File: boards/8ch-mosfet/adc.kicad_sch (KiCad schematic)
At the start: 13 parts, among them U13 MCP1502-33, U15 MCP3425A0T-ECH, U2 MCP3208

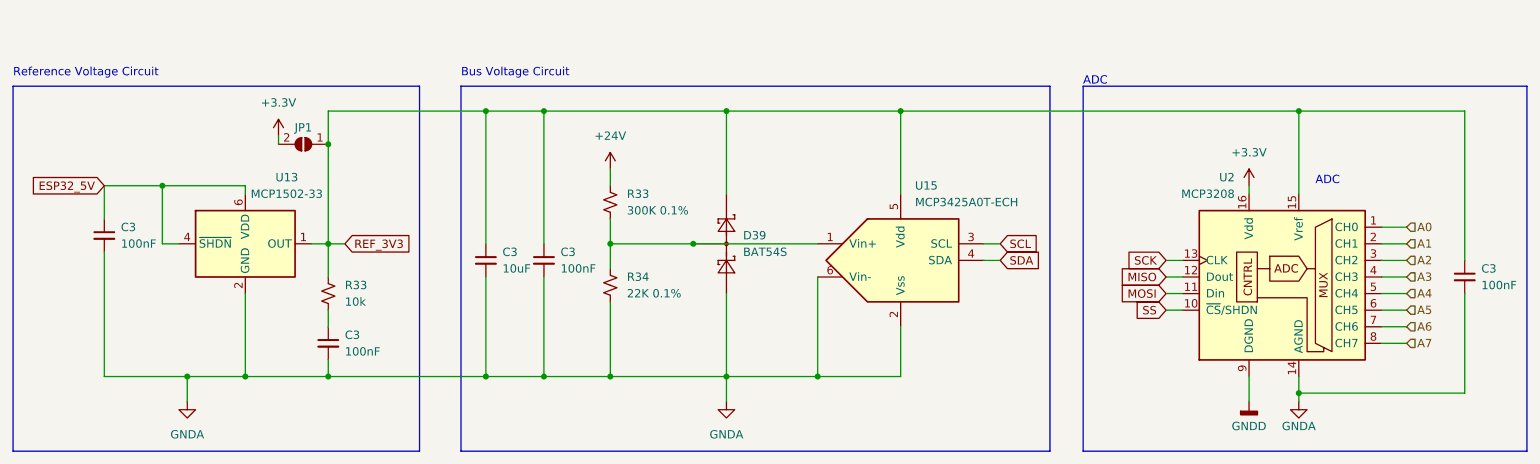
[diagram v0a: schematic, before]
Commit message: updated mosfet driver schematic with changes
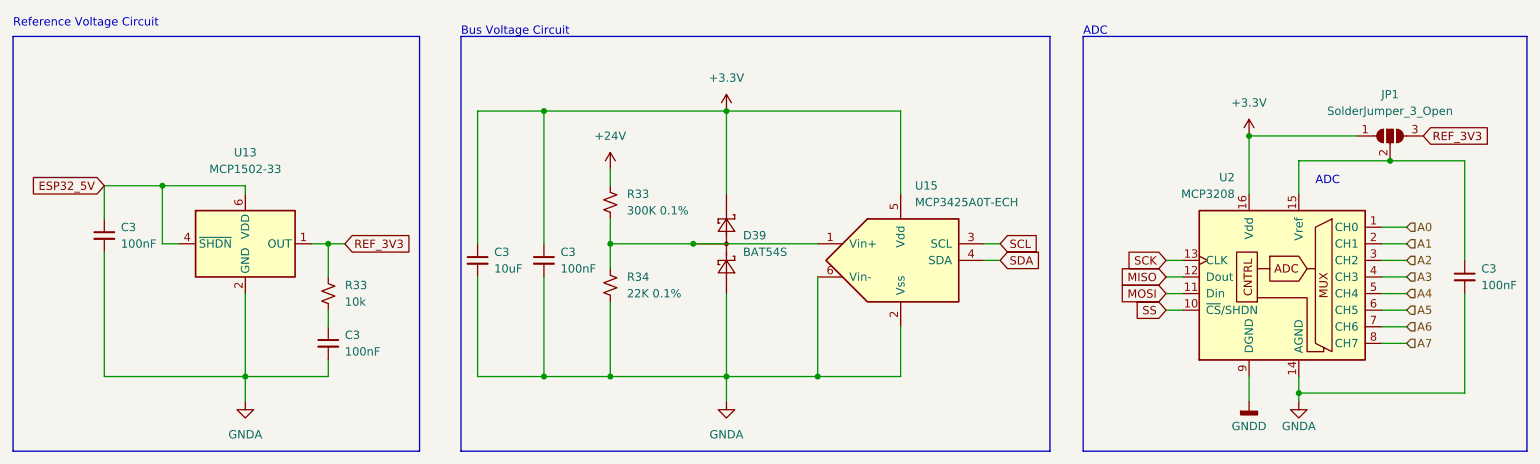
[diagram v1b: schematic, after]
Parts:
- removed JP1: SolderJumper_2_Open, Jumper:SolderJumper-2_P1.3mm_Open_RoundedPad1.0x1.5mm, symbol Jumper:SolderJumper_2_Open
- added JP1: SolderJumper_3_Open, Jumper:SolderJumper-3_P1.3mm_Open_RoundedPad1.0x1.5mm_NumberLabels, symbol Jumper:SolderJumper_3_Open
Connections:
- net +3.3V: now also C3.1, C3.1, D39.2 (K), U15.5 (Vdd), JP1.1 (A)
- net REF_3V3: now also JP1.3 (B); no longer C3.1, C3.1, C3.1, D39.2 (K), U15.5 (Vdd), U2.15 (Vref)
- new net: C3.1, JP1.2 (C), U2.15 (Vref)
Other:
- moved on the sheet: C3

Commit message: reannotated
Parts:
- renumbered D39 to D21, U13 to U18, U15 to U19
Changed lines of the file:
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@@
         )
         (path "/c83c6236-96e9-46ad-9d7a-9e2efa4a7966/b87f80e1-ecbd-4ee0-be26-4b252158928b"
-          (reference "U2") (unit 1)
+          (reference "U20") (unit 1)
         )
       )
@@
         )
         (path "/c83c6236-96e9-46ad-9d7a-9e2efa4a7966/b87f80e1-ecbd-4ee0-be26-4b252158928b"
-          (reference "#PWR07") (unit 1)
+          (reference "#PWR056") (unit 1)
         )
       )
@@
         )
         (path "/c83c6236-96e9-46ad-9d7a-9e2efa4a7966/b87f80e1-ecbd-4ee0-be26-4b252158928b"
-          (reference "#PWR03") (unit 1)
+          (reference "#PWR054") (unit 1)
         )
       )
@@
         )
         (path "/c83c6236-96e9-46ad-9d7a-9e2efa4a7966/b87f80e1-ecbd-4ee0-be26-4b252158928b"
-          (reference "#PWR070") (unit 1)
+          (reference "#PWR053") (unit 1)
         )
       )
@@
         )
         (path "/c83c6236-96e9-46ad-9d7a-9e2efa4a7966/b87f80e1-ecbd-4ee0-be26-4b252158928b"
-          (reference "R33") (unit 1)
+          (reference "R28") (unit 1)
         )
       )
@@
         )
         (path "/c83c6236-96e9-46ad-9d7a-9e2efa4a7966/b87f80e1-ecbd-4ee0-be26-4b252158928b"
-          (reference "R41") (unit 1)
+          (reference "R30") (unit 1)
         )
       )
@@
         )
         (path "/c83c6236-96e9-46ad-9d7a-9e2efa4a7966/b87f80e1-ecbd-4ee0-be26-4b252158928b"
-          (reference "#PWR058") (unit 1)
+          (reference "#PWR050") (unit 1)
         )
       )
@@
         )
         (path "/c83c6236-96e9-46ad-9d7a-9e2efa4a7966/b87f80e1-ecbd-4ee0-be26-4b252158928b"
-          (reference "C49") (unit 1)
+          (reference "C36") (unit 1)
         )
       )
@@
         )
         (path "/c83c6236-96e9-46ad-9d7a-9e2efa4a7966/b87f80e1-ecbd-4ee0-be26-4b252158928b"
-          (reference "#PWR057") (unit 1)
+          (reference "#PWR051") (unit 1)
         )
       )
@@
         )
         (path "/c83c6236-96e9-46ad-9d7a-9e2efa4a7966/b87f80e1-ecbd-4ee0-be26-4b252158928b"
-          (reference "#PWR06") (unit 1)
+          (reference "#PWR055") (unit 1)
         )
       )
@@
   (symbol (lib_id "Reference_Voltage:MCP1501-30xCH") (at 71.12 82.55 0) (unit 1)
     (in_bom yes) (on_board yes) (dnp no)
-    (property "Reference" "U13" (at 71.12 68.58 0)
+    (property "Reference" "U18" (at 71.12 68.58 0)
       (effects (font (size 1.27 1.27)))
     )
@@
       (project "8ch-mosfet"
         (path "/c83c6236-96e9-46ad-9d7a-9e2efa4a7966/b87f80e1-ecbd-4ee0-be26-4b252158928b"
-          (reference "U13") (unit 1)
+          (reference "U18") (unit 1)
         )
       )
@@
         )
         (path "/c83c6236-96e9-46ad-9d7a-9e2efa4a7966/b87f80e1-ecbd-4ee0-be26-4b252158928b"
-          (reference "C48") (unit 1)
+          (reference "C34") (unit 1)
         )
       )
@@
         )
         (path "/c83c6236-96e9-46ad-9d7a-9e2efa4a7966/b87f80e1-ecbd-4ee0-be26-4b252158928b"
-          (reference "#PWR010") (unit 1)
+          (reference "#PWR052") (unit 1)
         )
       )
@@
         )
         (path "/c83c6236-96e9-46ad-9d7a-9e2efa4a7966/b87f80e1-ecbd-4ee0-be26-4b252158928b"
-          (reference "C30") (unit 1)
+          (reference "C37") (unit 1)
         )
       )
@@
   (symbol (lib_id "Analog_ADC:MCP3425A0T-ECH") (at 171.45 85.09 0) (unit 1)
     (in_bom yes) (on_board yes) (dnp no) (fields_autoplaced)
-    (property "Reference" "U15" (at 173.6441 73.66 0)
+    (property "Reference" "U19" (at 173.6441 73.66 0)
       (effects (font (size 1.27 1.27)) (justify left))
     )
@@
       (project "8ch-mosfet"
         (path "/c83c6236-96e9-46ad-9d7a-9e2efa4a7966/b87f80e1-ecbd-4ee0-be26-4b252158928b"
-          (reference "U15") (unit 1)
+          (reference "U19") (unit 1)
         )
       )
@@
         )
         (path "/c83c6236-96e9-46ad-9d7a-9e2efa4a7966/b87f80e1-ecbd-4ee0-be26-4b252158928b"
-          (reference "C28") (unit 1)
+          (reference "C35") (unit 1)
         )
       )
@@
         )
         (path "/c83c6236-96e9-46ad-9d7a-9e2efa4a7966/b87f80e1-ecbd-4ee0-be26-4b252158928b"
-          (reference "R34") (unit 1)
+          (reference "R29") (unit 1)
         )
       )
@@
   (symbol (lib_id "Diode:BAT54S") (at 144.78 82.55 270) (mirror x) (unit 1)
     (in_bom yes) (on_board yes) (dnp no) (fields_autoplaced)
-    (property "Reference" "D39" (at 147.32 81.28 90)
+    (property "Reference" "D21" (at 147.32 81.28 90)
       (effects (font (size 1.27 1.27)) (justify left))
     )
@@
       (project "8ch-mosfet"
         (path "/c83c6236-96e9-46ad-9d7a-9e2efa4a7966/b87f80e1-ecbd-4ee0-be26-4b252158928b"
-          (reference "D39") (unit 1)
+          (reference "D21") (unit 1)
         )
       )
@@
         )
         (path "/c83c6236-96e9-46ad-9d7a-9e2efa4a7966/b87f80e1-ecbd-4ee0-be26-4b252158928b"
-          (reference "C29") (unit 1)
-        )
-      )
+          (reference "C33") (unit 1)
+        )
+      )

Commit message: 8 channel mosfet driver also ready for proto
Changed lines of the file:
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@@
   (title_block
     (title "Yarrboard 8ch Mosfet Driver")
+    (rev "C")
     (company "https://github.com/hoeken/yarrboard")
   )
@@
   )
   (junction (at 232.41 105.41) (diameter 0) (color 0 0 0 0)
+  )
+  (junction (at 232.41 69.85) (diameter 0) (color 0 0 0 0)
   )
   (junction (at 127 102.87) (diameter 0) (color 0 0 0 0)
@@
         )
       )
+    )
+  )
+  (symbol (lib_id "power:PWR_FLAG") (at 232.41 69.85 0) (unit 1)
+    (in_bom yes) (on_board yes) (dnp no)
+    (property "Reference" "#FLG04" (at 232.41 67.945 0)
+      (effects (font (size 1.27 1.27)) hide)
+    )
+    (property "Value" "PWR_FLAG" (at 232.41 71.12 0)
+      (effects (font (size 1.27 1.27)))
+    )
+    (property "Footprint" "" (at 232.41 69.85 0)
+      (effects (font (size 1.27 1.27)) hide)
+    )
+    (property "Datasheet" "~" (at 232.41 69.85 0)
+      (effects (font (size 1.27 1.27)) hide)
+    )
+    (pin "1")
+    (instances
+      (project "8ch-mosfet"
+        (path "/c83c6236-96e9-46ad-9d7a-9e2efa4a7966/e112a34f-fd2f-43cb-bf5d-a7f5e57b6bef"
+          (reference "#FLG04") (unit 1)
+        )
+        (path "/c83c6236-96e9-46ad-9d7a-9e2efa4a7966/b87f80e1-ecbd-4ee0-be26-4b252158928b"
+          (reference "#FLG010") (unit 1)
+        )
+      )

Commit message: first commit of the 'totem pole' driver design
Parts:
- removed JP1: SolderJumper_3_Open, Jumper:SolderJumper-3_P1.3mm_Open_RoundedPad1.0x1.5mm_NumberLabels, symbol Jumper:SolderJumper_3_Open
- added JP1: SolderJumper_2_Open, Jumper:SolderJumper-2_P1.3mm_Open_RoundedPad1.0x1.5mm, symbol Jumper:SolderJumper_2_Open
- renumbered D21 to D39, U18 to U13, U19 to U15
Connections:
- net +3.3V: now also JP1.2 (B); no longer C3.1, C3.1, D39.2 (K), U15.5 (Vdd)
- net REF_3V3: now also C3.1, C3.1, C3.1, D39.2 (K), U15.5 (Vdd), U2.15 (Vref), JP1.1 (A)
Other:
- moved on the sheet: C3

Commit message: oof, working from the wrong copy, had to redo some stuff
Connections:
- net +3.3V: now also C3.1, C3.1, D39.2 (K), U15.5 (Vdd)
- net REF_3V3: no longer C3.1, C3.1, D39.2 (K), U15.5 (Vdd)
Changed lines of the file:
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@@
   (title_block
     (title "Yarrboard 8ch Mosfet Driver")
+    (rev "C1")
     (company "https://github.com/hoeken/yarrboard")
   )
-  (junction (at 107.95 102.87) (diameter 0) (color 0 0 0 0)
-  )
   (junction (at 144.78 102.87) (diameter 0) (color 0 0 0 0)
   )
   (junction (at 158.75 102.87) (diameter 0) (color 0 0 0 0)
   )
-  (junction (at 83.82 67.31) (diameter 0) (color 0 0 0 0)
-  )
-  (junction (at 232.41 62.23) (diameter 0) (color 0 0 0 0)
-  )
   (junction (at 232.41 105.41) (diameter 0) (color 0 0 0 0)
   )
-  (junction (at 107.95 62.23) (diameter 0) (color 0 0 0 0)
+  (junction (at 245.11 69.85) (diameter 0) (color 0 0 0 0)
   )
   (junction (at 127 102.87) (diameter 0) (color 0 0 0 0)
@@
   (junction (at 83.82 82.55) (diameter 0) (color 0 0 0 0)
   )
-  (junction (at 83.82 102.87) (diameter 0) (color 0 0 0 0)
-  )
-  (junction (at 171.45 62.23) (diameter 0) (color 0 0 0 0)
-  )
   (junction (at 58.42 73.66) (diameter 0) (color 0 0 0 0)
   )
@@
     (stroke (width 0) (type default))
   )
-  (wire (pts (xy 232.41 62.23) (xy 257.81 62.23))
+  (wire (pts (xy 232.41 69.85) (xy 245.11 69.85))
     (stroke (width 0) (type default))
   )
@@
     (stroke (width 0) (type default))
   )
-  (wire (pts (xy 257.81 62.23) (xy 257.81 85.09))
+  (wire (pts (xy 257.81 69.85) (xy 257.81 85.09))
     (stroke (width 0) (type default))
   )
@@
     (stroke (width 0) (type default))
   )
+  (wire (pts (xy 245.11 64.77) (xy 245.11 69.85))
+    (stroke (width 0) (type default))
+  )
   (wire (pts (xy 58.42 73.66) (xy 58.42 82.55))
     (stroke (width 0) (type default))
@@
     (stroke (width 0) (type default))
   )
-  (wire (pts (xy 83.82 102.87) (xy 107.95 102.87))
-    (stroke (width 0) (type default))
-  )
   (wire (pts (xy 232.41 105.41) (xy 232.41 106.68))
     (stroke (width 0) (type default))
@@
     (stroke (width 0) (type default))
   )
-  (wire (pts (xy 83.82 62.23) (xy 83.82 67.31))
-    (stroke (width 0) (type default))
-  )
   (wire (pts (xy 212.09 87.63) (xy 214.63 87.63))
     (stroke (width 0) (type default))
@@
     (stroke (width 0) (type default))
   )
-  (wire (pts (xy 171.45 62.23) (xy 232.41 62.23))
-    (stroke (width 0) (type default))
-  )
   (wire (pts (xy 49.53 83.82) (xy 49.53 102.87))
     (stroke (width 0) (type default))
@@
     (stroke (width 0) (type default))
   )
-  (wire (pts (xy 83.82 62.23) (xy 107.95 62.23))
-    (stroke (width 0) (type default))
-  )
   (wire (pts (xy 49.53 102.87) (xy 62.23 102.87))
     (stroke (width 0) (type default))
@@
     (stroke (width 0) (type default))
   )
+  (wire (pts (xy 245.11 69.85) (xy 257.81 69.85))
+    (stroke (width 0) (type default))
+  )
   (wire (pts (xy 245.11 87.63) (xy 248.92 87.63))
     (stroke (width 0) (type default))
@@
     (stroke (width 0) (type default))
   )
-  (wire (pts (xy 232.41 62.23) (xy 232.41 74.93))
+  (wire (pts (xy 232.41 69.85) (xy 232.41 74.93))
     (stroke (width 0) (type default))
   )
@@
     (stroke (width 0) (type default))
   )
-  (wire (pts (xy 224.79 73.66) (xy 224.79 74.93))
+  (wire (pts (xy 224.79 67.31) (xy 224.79 74.93))
     (stroke (width 0) (type default))
   )
@@
     (stroke (width 0) (type default))
   )
-  (rectangle (start 199.39 58.42) (end 267.335 114.3)
+  (rectangle (start 199.39 50.8) (end 267.335 114.3)
     (stroke (width 0) (type default))
     (fill (type none))
   )
-  (rectangle (start 35.56 58.42) (end 97.79 114.3)
+  (rectangle (start 35.56 50.8) (end 97.79 114.3)
     (stroke (width 0) (type default))
     (fill (type none))
   )
-  (rectangle (start 104.14 58.42) (end 194.31 114.3)
+  (rectangle (start 104.14 50.8) (end 194.31 114.3)
     (stroke (width 0) (type default))
     (fill (type none))
   )
-  (text "ADC\n" (at 199.39 58.42 0)
+  (text "ADC\n" (at 199.39 50.8 0)
     (effects (font (size 1.27 1.27)) (justify left bottom))
   )
@@
     (effects (font (size 1.27 1.27)) (justify left bottom))
   )
-  (text "Bus Voltage Circuit" (at 104.14 57.15 0)
+  (text "Bus Voltage Circuit" (at 104.14 50.8 0)
     (effects (font (size 1.27 1.27)) (justify left bottom))
   )
-  (text "Reference Voltage Circuit" (at 35.56 57.15 0)
+  (text "Reference Voltage Circuit" (at 35.56 50.8 0)
     (effects (font (size 1.27 1.27)) (justify left bottom))
   )
@@
     (property "Intersheetrefs" "${INTERSHEET_REFS}" (at 204.5086 87.63 0)
       (effects (font (size 1.27 1.27)) (justify right) hide)
+    )
+  )
+  (global_label "REF_3V3" (shape input) (at 245.11 64.77 0) (fields_autoplaced)
+    (effects (font (size 1.27 1.27)) (justify left))
+    (property "Intersheetrefs" "${INTERSHEET_REFS}" (at 256.078 64.77 0)
+      (effects (font (size 1.27 1.27)) (justify left) hide)
     )
   )
@@
     )
   )
-  (symbol (lib_id "power:+3.3V") (at 224.79 73.66 0) (unit 1)
-    (in_bom yes) (on_board yes) (dnp no) (fields_autoplaced)
-    (property "Reference" "#PWR02" (at 224.79 77.47 0)
-      (effects (font (size 1.27 1.27)) hide)
-    )
-    (property "Value" "+3.3V" (at 224.79 68.58 0)
+  (symbol (lib_id "power:+3.3V") (at 224.79 67.31 0) (unit 1)
+    (in_bom yes) (on_board yes) (dnp no) (fields_autoplaced)
+    (property "Reference" "#PWR02" (at 224.79 71.12 0)
+      (effects (font (size 1.27 1.27)) hide)
+    )
+    (property "Value" "+3.3V" (at 224.79 62.23 0)
       (effects (font (size 1.27 1.27)))
     )
-    (property "Footprint" "" (at 224.79 73.66 0)
-      (effects (font (size 1.27 1.27)) hide)
-    )
-    (property "Datasheet" "" (at 224.79 73.66 0)
+    (property "Footprint" "" (at 224.79 67.31 0)
+      (effects (font (size 1.27 1.27)) hide)
+    )
+    (property "Datasheet" "" (at 224.79 67.31 0)
       (effects (font (size 1.27 1.27)) hide)
     )
@@
         )
       )
+    )
+  )
+  (symbol (lib_id "power:+3.3V") (at 144.78 62.23 0) (unit 1)
+    (in_bom yes) (on_board yes) (dnp no) (fields_autoplaced)
+    (property "Reference" "#PWR02" (at 144.78 66.04 0)
+      (effects (font (size 1.27 1.27)) hide)
+    )
+    (property "Value" "+3.3V" (at 144.78 57.15 0)
+      (effects (font (size 1.27 1.27)))
+    )
+    (property "Footprint" "" (at 144.78 62.23 0)
+      (effects (font (size 1.27 1.27)) hide)
+    )
+    (property "Datasheet" "" (at 144.78 62.23 0)
+      (effects (font (size 1.27 1.27)) hide)
+    )
+    (pin "1")
+    (instances
+      (project "8ch-mosfet"
+        (path "/c83c6236-96e9-46ad-9d7a-9e2efa4a7966"
+          (reference "#PWR02") (unit 1)
+        )
+        (path "/c83c6236-96e9-46ad-9d7a-9e2efa4a7966/b87f80e1-ecbd-4ee0-be26-4b252158928b"
+          (reference "#PWR060") (unit 1)
+        )
+      )
